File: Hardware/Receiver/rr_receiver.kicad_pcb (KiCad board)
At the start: 2 copper layers, 38.5 x 21.5 mm, 23 parts, among them U1 AMS1117-3.3, U2 ATmega328P-A, U3 NRF24L01_Breakout, Y1 16MHz

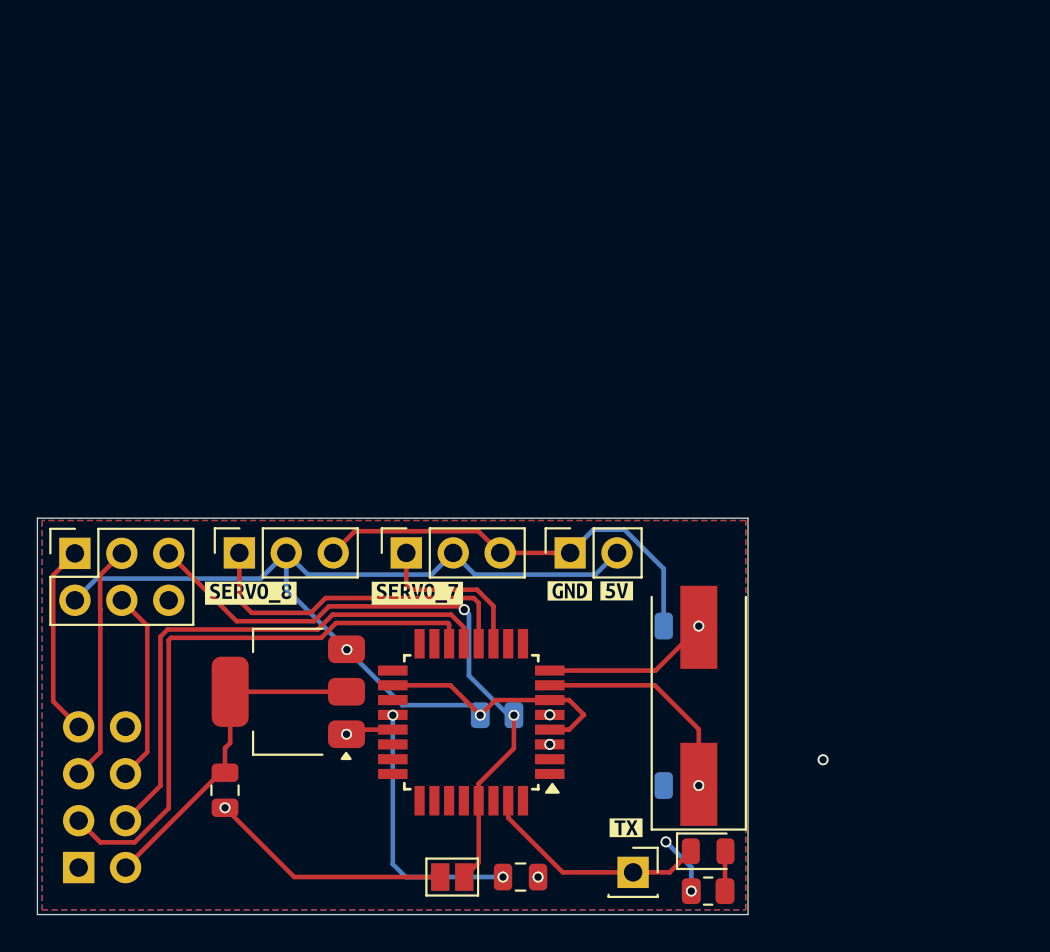
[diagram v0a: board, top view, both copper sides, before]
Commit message: update receiver because the old one doesn't work
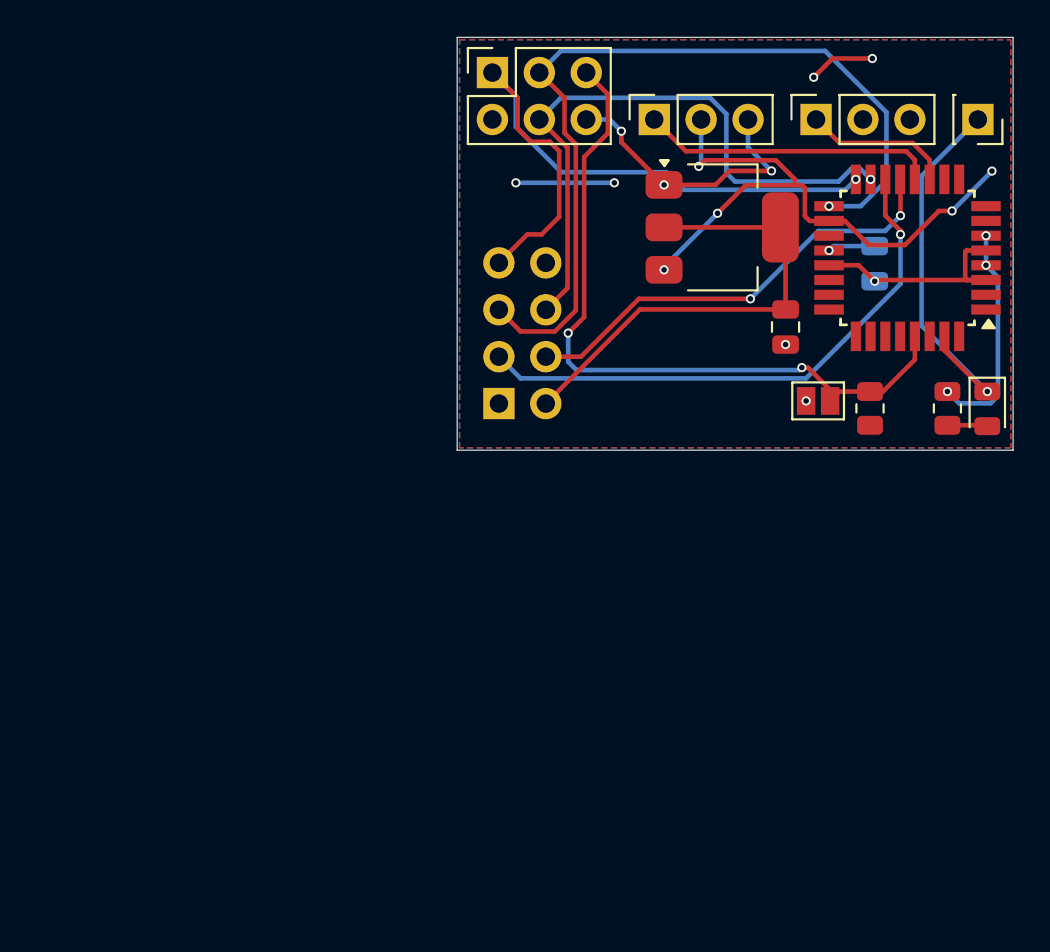
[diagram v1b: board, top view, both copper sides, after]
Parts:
- removed C3, C4: 0.1, Capacitor_SMD:C_0805_2012Metric
- removed ICSP: ICSP, Connector_PinSocket_2.54mm:PinSocket_2x03_P2.54mm_Vertical
- removed RST: RSTJUMP, Jumper:SolderJumper-2_P1.3mm_Open_Pad1.0x1.5mm
- removed SRV_8: SERVO1, Connector_PinSocket_2.54mm:PinSocket_1x03_P2.54mm_Vertical
- removed SRV_8: SERVO2, Connector_PinSocket_2.54mm:PinSocket_1x03_P2.54mm_Vertical
- removed TX: TX, Connector_PinSocket_2.54mm:PinSocket_1x01_P2.54mm_Vertical
- removed VCC: POWER, Connector_PinSocket_2.54mm:PinSocket_1x02_P2.54mm_Vertical
- removed Y1: 16MHz, Crystal:Crystal_SMD_HC49-SD
- removed kibuzzard-6781DEB8: G***, kibuzzard-6781DEB8
- removed kibuzzard-6781DECC: G***, kibuzzard-6781DECC
- removed kibuzzard-6781DEDE: G***, kibuzzard-6781DEDE
- removed kibuzzard-6781DF01: G***, kibuzzard-6781DF01
- removed kibuzzard-6781DF0B: G***, kibuzzard-6781DF0B
- removed kibuzzard-6781E9A8: G***, kibuzzard-6781E9A8
- added J1: TX, Connector_PinSocket_2.54mm:PinSocket_1x01_P2.54mm_Vertical, F.Cu at (168.4, 39.1)
- added J2: SERVO1, Connector_PinSocket_2.54mm:PinSocket_1x03_P2.54mm_Vertical, F.Cu at (159.6, 39.1)
- added J4: SERVO2, Connector_PinSocket_2.54mm:PinSocket_1x03_P2.54mm_Vertical, F.Cu at (150.9, 39.1)
- added J5: ICSP, Connector_PinSocket_2.54mm:PinSocket_2x03_P2.54mm_Vertical, F.Cu at (142.1, 36.6)
- added JP1: RSTJUMP, Jumper:SolderJumper-2_P1.3mm_Open_Pad1.0x1.5mm, F.Cu at (159.8, 54.4)
- C2: moved to B.Cu
- R2: moved to F.Cu
- moved C1 39.4 mm to (158.0, 50.4)
- moved C2 38.4 mm to (162.8, 46.9), turned to -90 degrees
- moved U2 34.5 mm to (164.6, 46.6)
- moved U1 34.4 mm to (154.6, 45.0), turned to 0 degrees
- moved U3 33.9 mm to (142.5, 54.5)
- moved R1 29.2 mm to (166.8, 54.8), turned to -90 degrees
- moved D1 28.3 mm to (168.9, 54.8), turned to -90 degrees
- moved R2 26.1 mm to (162.6, 54.8), turned to -90 degrees
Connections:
- U2 pad 15: unconnected-(U2-PB3-Pad15) -> /MOSI
- U2 pad 16: unconnected-(U2-PB4-Pad16) -> /MISO
- U2 pad 17: unconnected-(U2-PB5-Pad17) -> /SCK
- U2 pad 7: Net-(U2-XTAL1/PB6) -> unconnected-(U2-XTAL1/PB6-Pad7)
- U2 pad 8: Net-(U2-XTAL2/PB7) -> unconnected-(U2-XTAL2/PB7-Pad8)
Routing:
- net /SCK: track 12.9 -> 46.9 mm, vias 0 -> 1
- net /MISO: track 10.5 -> 37.7 mm, vias 0 -> 1
- net /MOSI: track 10.5 -> 34.1 mm, vias 0 -> 1
- net +5V: track 64.8 -> 49.8 mm, vias 4 -> 10
- net Net-(U2-XTAL1/PB6): track 12.2 -> 0.00 mm, vias 1 -> 0
- net Net-(U2-AREF): track 14.3 -> 2.57 mm, vias 2 -> 1
- net Net-(U2-XTAL2/PB7): track 9.27 -> 0.00 mm, vias 1 -> 0
- net /TX: track 12.5 -> 21.5 mm, vias 0 -> 1
- net +3.3V: track 18.3 -> 26.0 mm
- net GND: track 39.2 -> 31.7 mm, vias 5 -> 8
- net Net-(J5-~{RST}): track 34.8 -> 39.3 mm
- net Net-(U2-PB1): track 28.8 -> 24.3 mm, vias 0 -> 2
- net /SRV2: track 18.5 -> 16.1 mm
- net Net-(U2-PB2): track 31.9 -> 30.4 mm, vias 0 -> 1
- net /SRV1: track 8.92 -> 8.11 mm
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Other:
- board size 38.5 x 21.5 mm -> 30.1 x 22.4 mm
